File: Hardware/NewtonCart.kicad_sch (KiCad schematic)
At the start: 23 parts, among them J1 Battery Pins, J10 LOADCELL, J11 ON/OFF-Switch, J2 TP4056 Module, J3 Reserve IO's, J4 UART2TTL Bridge, J5 BoostConverter, J6 MPU6050, J7 HX711, J8 HC-SR04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

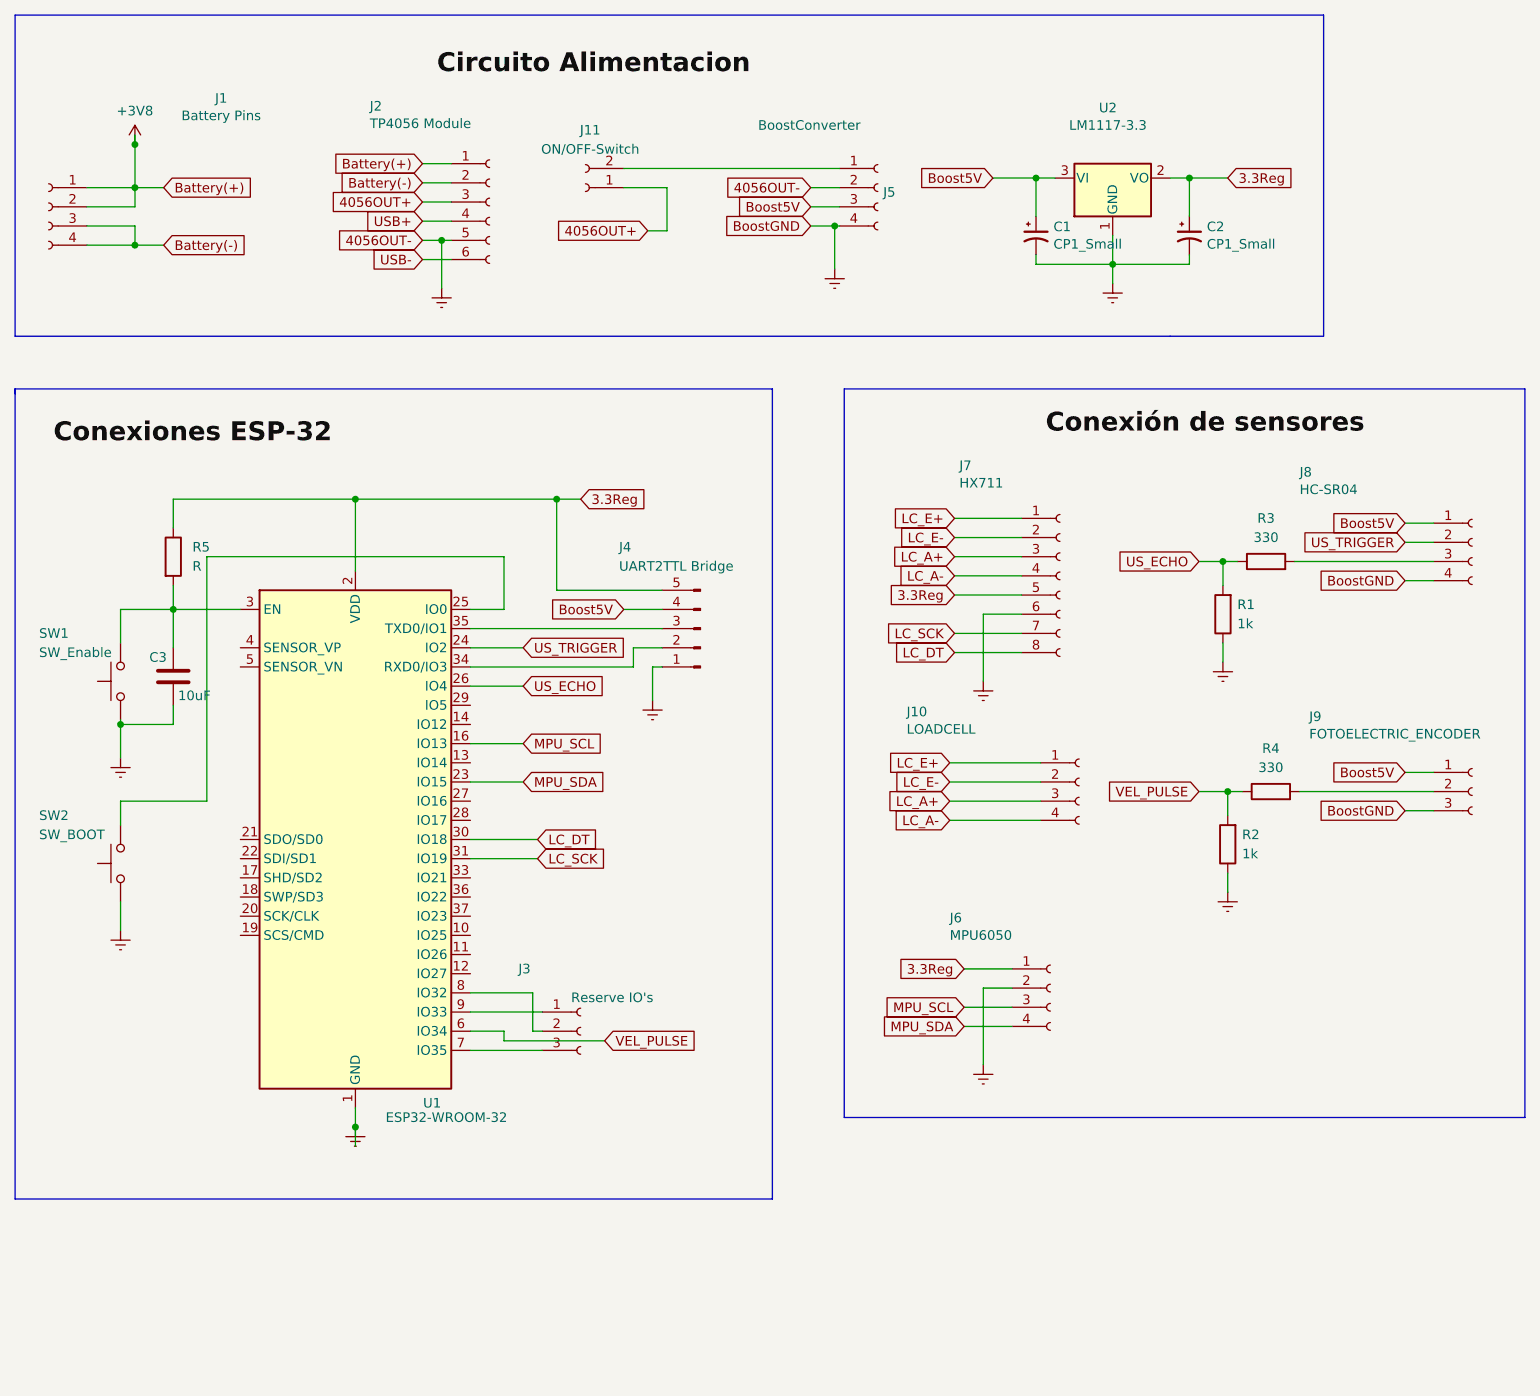
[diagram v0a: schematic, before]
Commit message: Final Changes to 3D design, added battery base, PCB place remarked, ON/OFF Switch and charging microUSB Slots. New holes in rowlock bases for internal wiring.   Updated NewtonCart firmware. New final code named "NewtonCartRTOS", in wich i merged the NewtonCart code and Bluetooth communication, additionaly the code is managed by the two ESP32 Cores by RTOS library.
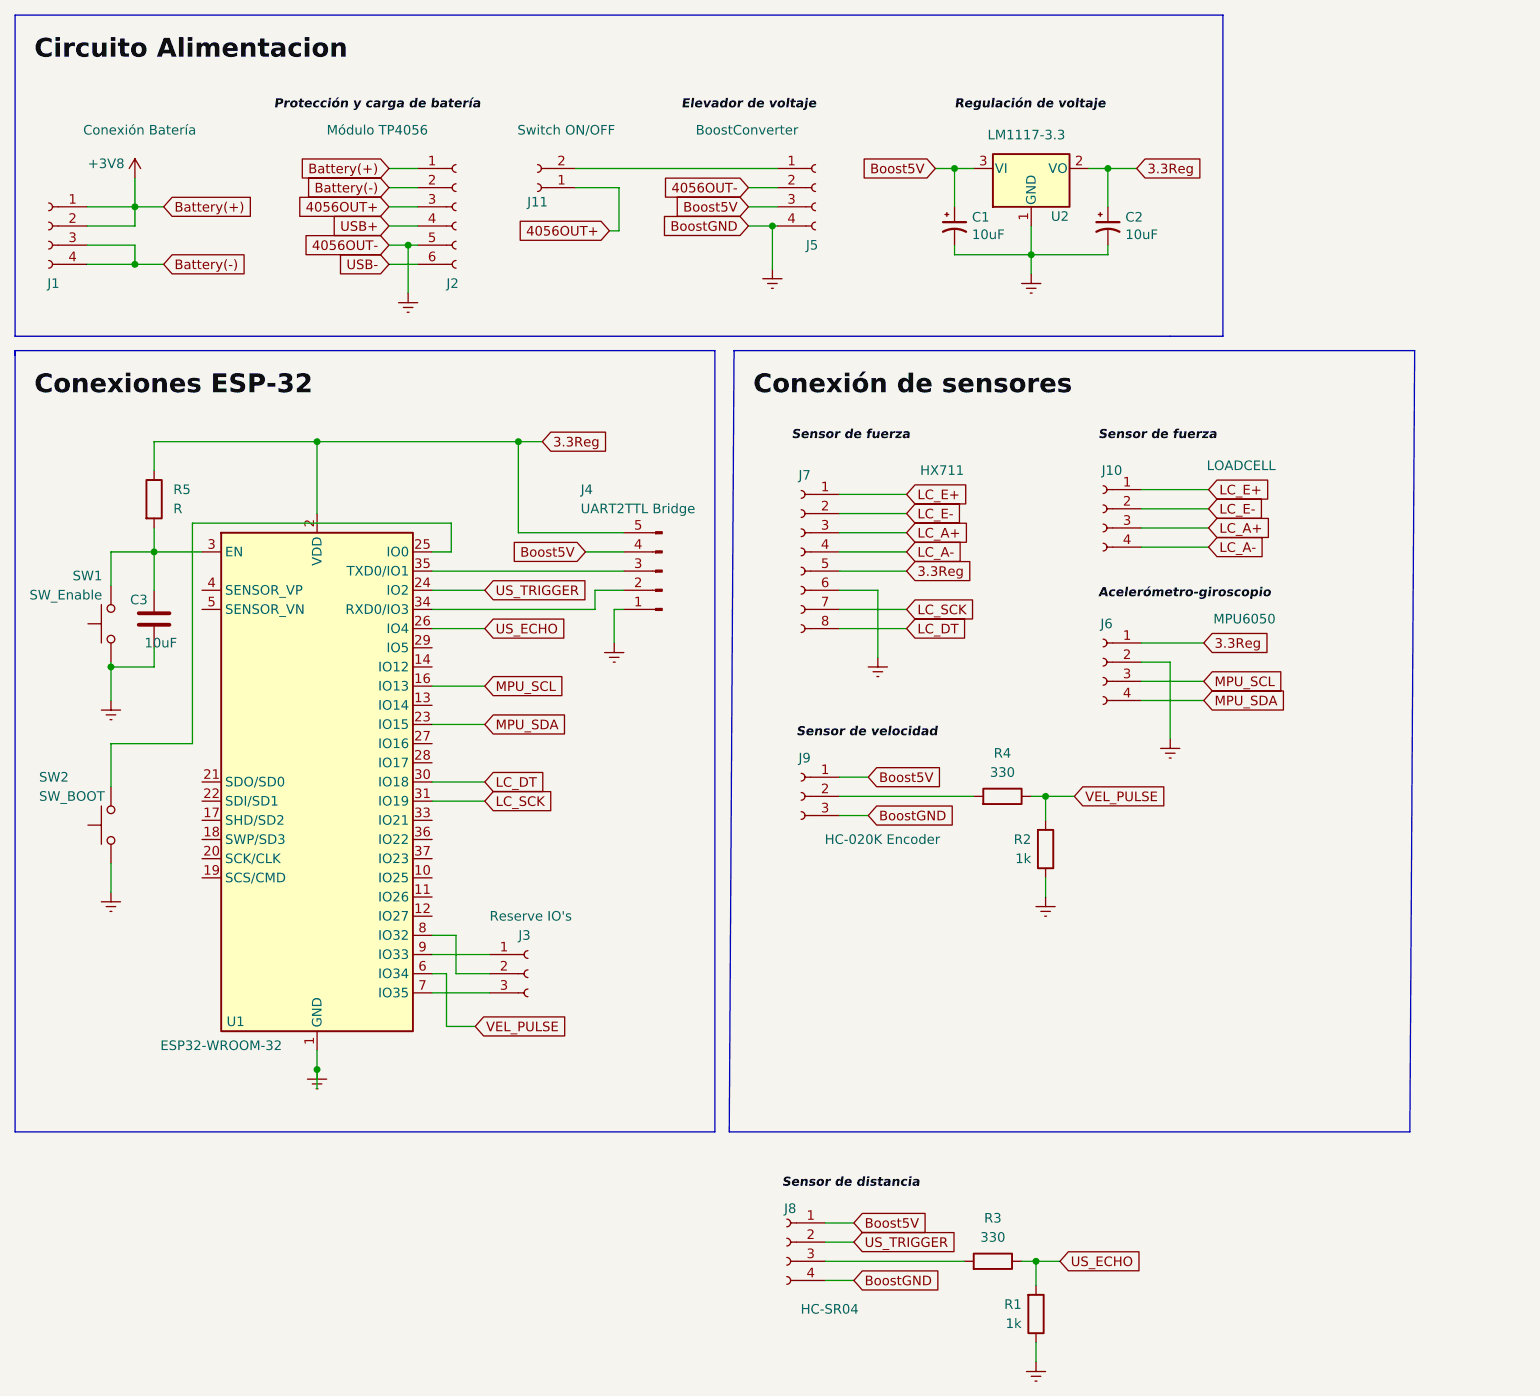
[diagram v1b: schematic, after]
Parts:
- C1, C2: value CP1_Small -> 10uF
- J1: value Battery Pins -> Conexión Batería
- J11: value ON/OFF-Switch -> Switch ON/OFF
- J2: value TP4056 Module -> Módulo TP4056
- J9: value FOTOELECTRIC_ENCODER -> HC-020K Encoder
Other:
- moved on the sheet: C1, C2, C3, J1, J10, J11, J2, J3, J4, J5, J6, J7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

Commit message: Se añadieron modelos 3D de sensores que fueron  utilizados para el análisis de centro de gravedad. Se añade funcionalidad RTOS en código Arduino Prototipo y programación funcional a este punto.
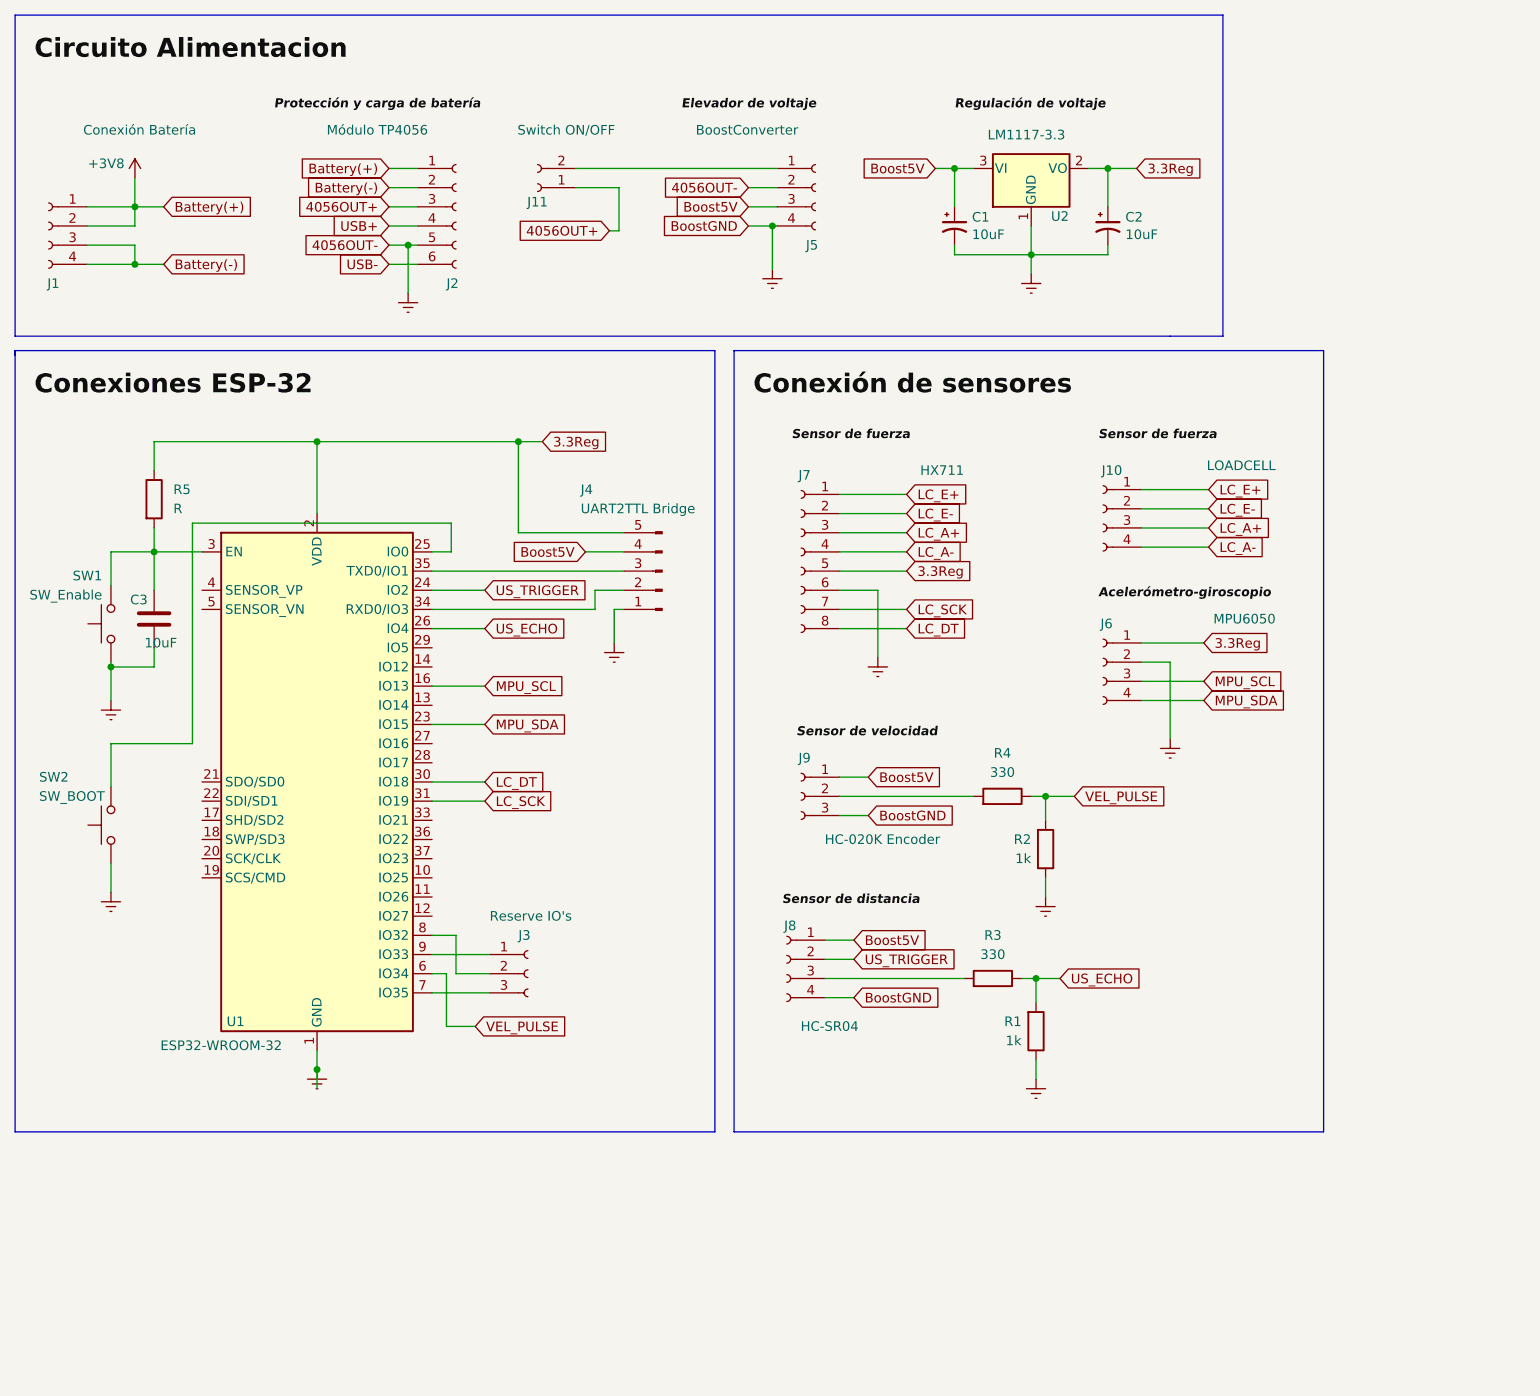
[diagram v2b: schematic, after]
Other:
- moved on the sheet: J8, R1, R3
